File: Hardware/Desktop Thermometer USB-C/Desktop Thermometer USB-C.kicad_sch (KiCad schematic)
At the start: 37 parts, among them J1 USB_TYPE_B, U1 74HC595, U2 74HC595, U3 74HC595, U4 TMP3x, U5 PIC16F15214

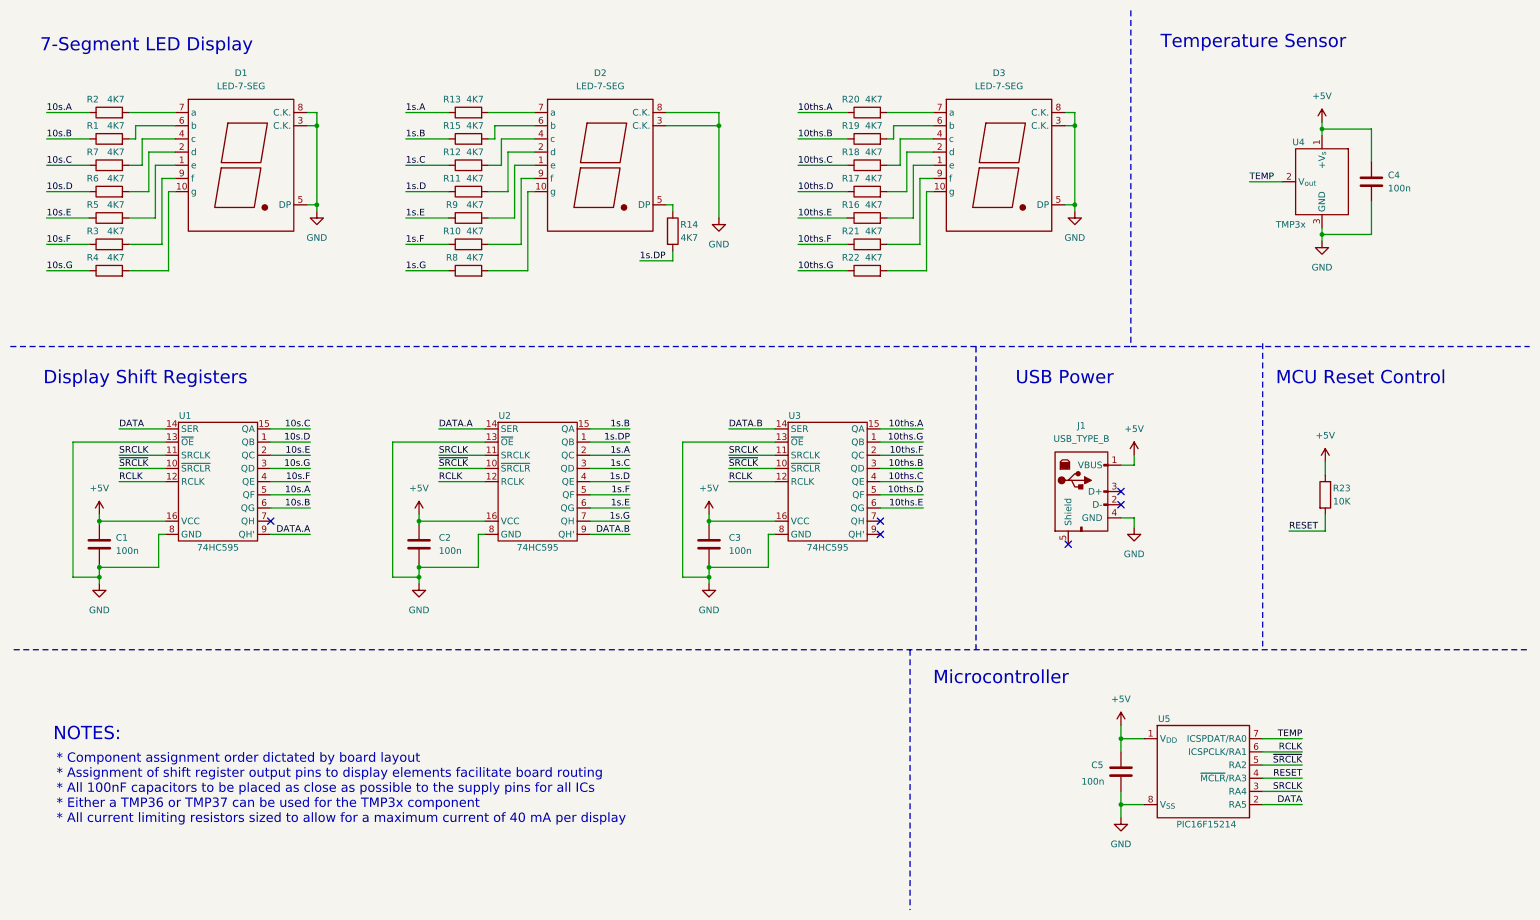
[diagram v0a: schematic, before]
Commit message: Updated the USB-C version of the schematic and updated the board to reflect changes
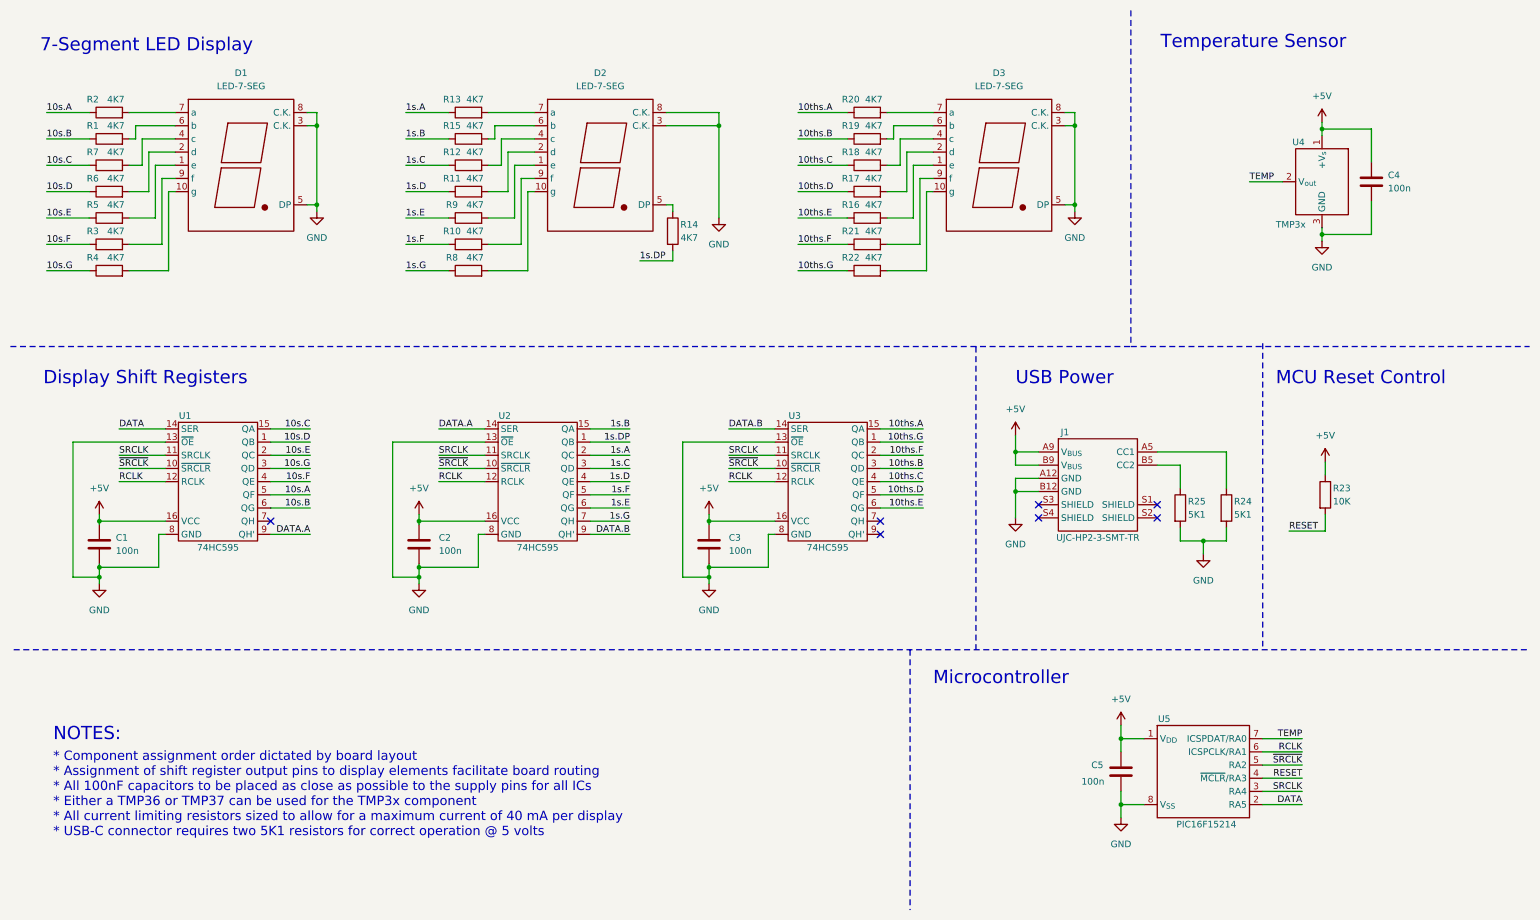
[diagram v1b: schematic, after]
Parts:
- removed J1: USB_TYPE_B, Footprints:USB_TYPE_B, symbol Schematic Symbols:USB_TYPE_B
- added J1: UJC-HP2-3-SMT-TR, Footprints:CUI_UJC-HP2-3-SMT-TR, symbol Schematic Symbols:USB_TYPE_C
- added R24, R25: 5K1, Resistor_THT:R_Axial_DIN0207_L6.3mm_D2.5mm_P10.16mm_Horizontal, symbol Device:R
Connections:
- net +5V: now also J1.A9 (V_{BUS}), J1.B9 (V_{BUS})
- net GND: now also J1.A12 (GND), J1.B12 (GND), R24.2, R25.2
- new net: J1.A5 (CC1), R24.1
- new net: J1.B5 (CC2), R25.1
- no-connect marks 6 -> 7
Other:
- note added: "* Component assignment order dictated by board layout * Assignment of shift register output pins to display elements facilitate board routing * All 100nF capacitors to be placed as close as possible to the supply pins for all ICs * Either a TMP36 or TMP37 can be used for the TMP3x component * All current limiting resistors sized to allow for a maximum current of 40 mA per display * USB-C connecto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"
- note removed: "* Component assignment order dictated by board layout * Assignment of shift register output pins to display elements facilitate board routing * All 100nF capacitors to be placed as close as possible to the supply pins for all ICs * Either a TMP36 or TMP37 can be used for the TMP3x component * All current limiting resistors sized to allow for a maximum current of 40 mA per display"

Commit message: Managed to get the footprint for the TMP3x device around the wrong way, this is now fixed. Also included data sheets for the PIC programmer and updates to the code configuration after testing.
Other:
- title: Desktop Thermometer - USB 2 Version -> Desktop Thermometer - USB C Version
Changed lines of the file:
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@@
   (paper "A4")
   (title_block
-    (title "Desktop Thermometer - USB 2 Version")
+    (title "Desktop Thermometer - USB C Version")
     (rev "1.0-A")
   )

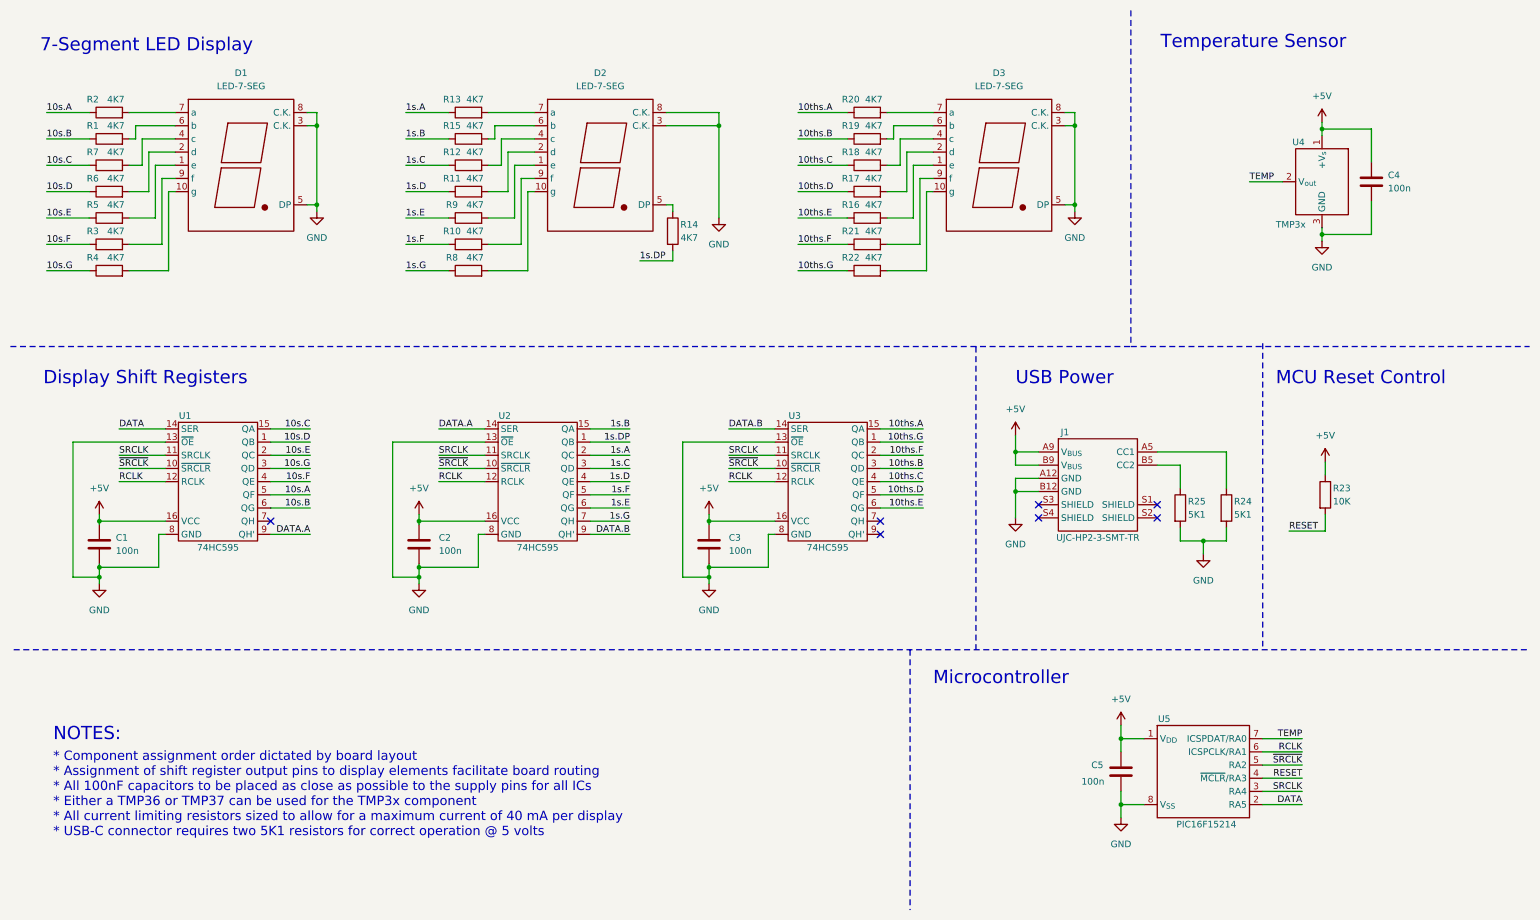
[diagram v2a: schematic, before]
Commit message: Finished PCB routing and generated GERBERS for both versions of the hardware.
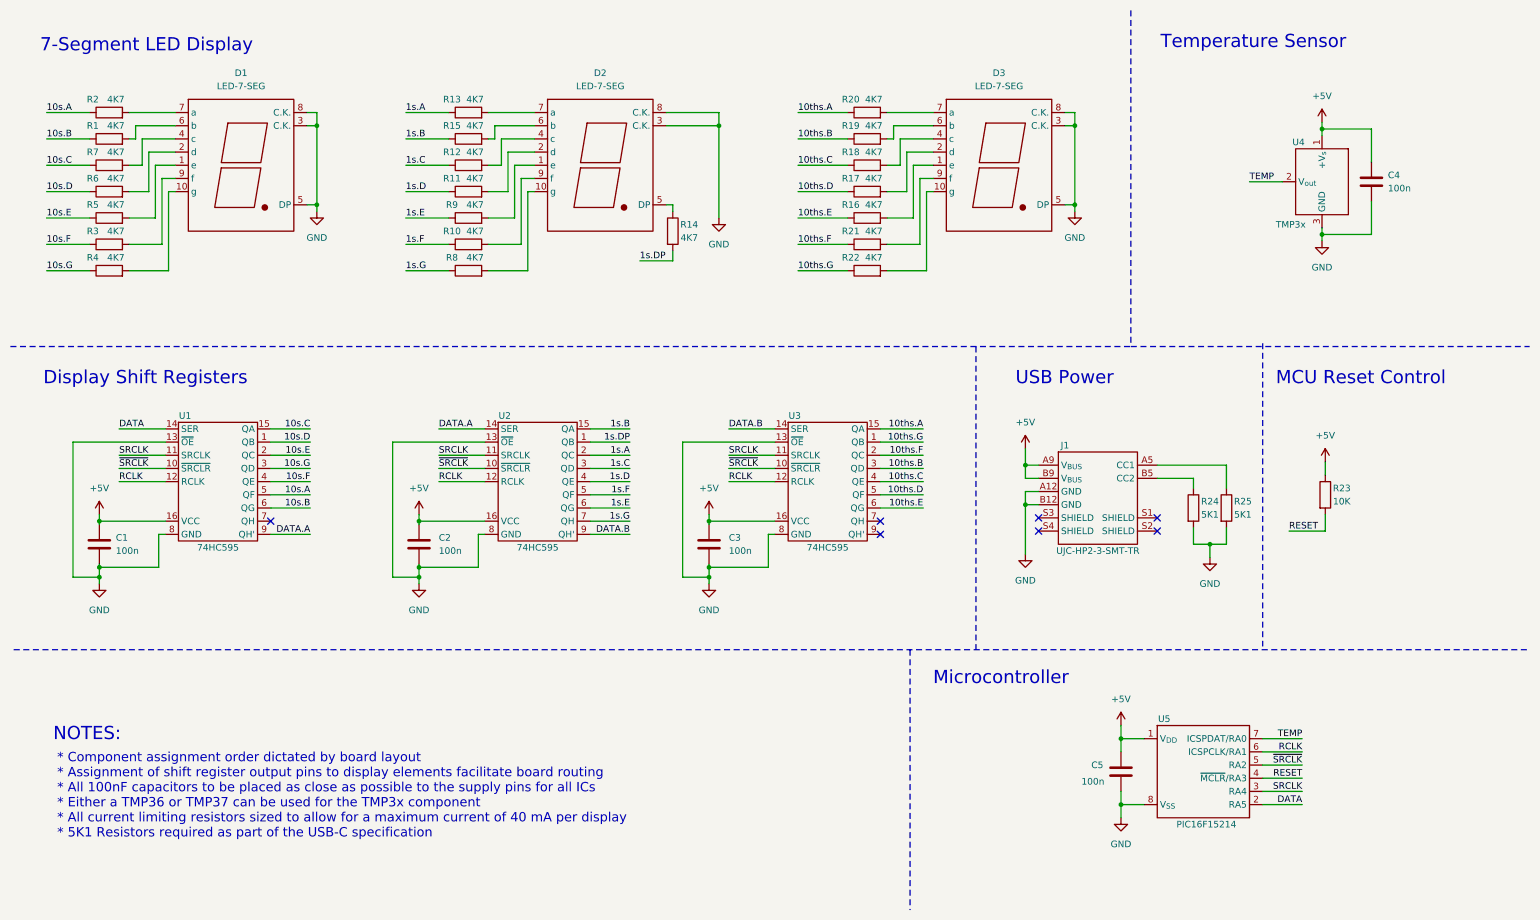
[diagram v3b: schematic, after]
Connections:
- net at J1.A5 (CC1): now also R25.1; no longer R24.1
- net at J1.B5 (CC2): now also R24.1; no longer R25.1
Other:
- note added: "* Component assignment order dictated by board layout * Assignment of shift register output pins to display elements facilitate board routing * All 100nF capacitors to be placed as close as possible to the supply pins for all ICs * Either a TMP36 or TMP37 can be used for the TMP3x component * All current limiting resistors sized to allow for a maximum current of 40 mA per display * 5K1 Resistors 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"
- note removed: "* Component assignment order dictated by board layout * Assignment of shift register output pins to display elements facilitate board routing * All 100nF capacitors to be placed as close as possible to the supply pins for all ICs * Either a TMP36 or TMP37 can be used for the TMP3x component * All current limiting resistors sized to allow for a maximum current of 40 mA per display * USB-C connecto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"
- title: Desktop Thermometer - USB C Version -> Desktop Thermometer - USB 2 Version
